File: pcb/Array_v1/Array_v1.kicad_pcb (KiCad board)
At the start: 4 copper layers, 430 parts, among them J1 D_ADC1, J11 D_VGA31, J12 D_VGA32, J13 D_ADC4, J14 GND, J16 D_VGA41, J17 D_VGA42, J18 VPOWER, J19 SPI_ADC, J2 MATCH1, J20 SPI_AGC_RX1, J21 SPI_AGC_RX2, J22 SPI_AGC_RX3, J23 SPI_AGC_RX4, J24 3.3VADC, J3 D_VGA11, J4 D_VGA11, J5 D_ADC2, J7 D_VGA21, J8 D_VGA22, J9 D_ADC3, U10 MEM, U11 DAC081S101, U12 AD8337, U13 ADS7040xDCU, U14 LMH6639, U15 CCSO-914X3-1000, U16 MAPD-009278, U17 MAPD-009278, U18 MAPD-009278, U19 CVSS-945-80.000, U2 TPS795, U20 MAPD-009278, U21 MAPD-009278, U22 MAPD-009278, U23 DAC081S101, U24 AD8337, U3 B39921, U4 SKY67159, U5 PAT0816, U6 PAT0816, U67 ADR391, U68 AD8541, U7 LT5526, U8 LT5526, U9 NFL

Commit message: can't run LVS meaningfully
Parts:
- removed the AE1 at (-81.4, 13.4)
- removed the AE1 at (-81.5, 166.5)
- removed the AE1 at (-234.6, 166.4)
- removed the AE1 at (-235.0, 12.8)
- removed the C10 at (-142.7, 66.7)
- removed the C10 at (-134.8, 105.2)
- removed the C10 at (-173.3, 113.1)
- removed the C10 at (-181.7, 74.1)
- removed the C11 at (-127.3, 50.7)
- removed the C11 at (-118.7, 120.6)
- removed the C11 at (-188.6, 129.2)
- removed the C11 at (-197.8, 58.8)
- removed the C12 at (-124.2, 48.2)
- removed the C12 at (-116.3, 123.7)
- removed the C12 at (-191.8, 131.6)
- removed the C12 at (-200.2, 55.6)
- removed the C13 at (-141.2, 78.5)
- removed the C13 at (-146.6, 106.7)
- removed the C13 at (-174.8, 101.4)
- removed the C13 at (-169.9, 72.6)
- removed the C14 at (-122.7, 60.0)
- removed the C14 at (-128.0, 125.2)
- removed the C14 at (-193.3, 119.9)
- removed the C14 at (-188.4, 54.1)
- removed the C15 at (-135.8, 69.1)
- removed the C15 at (-137.2, 112.1)
- removed the C15 at (-180.2, 110.7)
- removed the C15 at (-179.3, 67.2)
- removed the C16 at (-117.3, 50.6)
- removed the C16 at (-118.7, 130.6)
- removed the C16 at (-198.7, 129.2)
- removed the C16 at (-197.8, 48.7)
- removed the C17 at (-146.4, 78.3)
- removed the C17 at (-146.4, 101.5)
- removed the C17 at (-169.6, 101.5)
- removed the C17 at (-170.1, 77.8)
- removed the C18 at (-127.9, 59.8)
- removed the C18 at (-127.9, 120.0)
- removed the C18 at (-188.1, 120.0)
- removed the C18 at (-188.6, 59.3)
- removed the C19 at (-144.6, 75.1)
- removed the C19 at (-143.1, 103.3)
- removed the C19 at (-171.4, 104.8)
- removed the C19 at (-173.4, 76.0)
- removed the C20 at (-126.1, 56.6)
- removed the C20 at (-124.6, 121.8)
- removed the C20 at (-189.9, 123.3)
- removed the C20 at (-191.9, 57.5)
- removed the C21 at (-139.4, 65.5)
- removed the C21 at (-133.6, 108.5)
- removed the C21 at (-176.6, 114.3)
- removed the C21 at (-182.9, 70.8)
- removed the C22 at (-120.9, 47.0)
- removed the C22 at (-115.1, 127.0)
- removed the C22 at (-195.1, 132.8)
- removed the C22 at (-201.4, 52.3)
- removed the C23 at (-137.0, 76.5)
- removed the C23 at (-144.6, 110.9)
- removed the C23 at (-178.9, 103.3)
- removed the C23 at (-171.9, 68.5)
- removed the C24 at (-135.6, 75.1)
- removed the C24 at (-143.2, 112.3)
- removed the C24 at (-180.4, 104.7)
- removed the C24 at (-173.3, 67.0)
- removed the C25 at (-118.5, 58.0)
- removed the C25 at (-126.1, 129.4)
- removed the C25 at (-197.4, 121.8)
- removed the C25 at (-190.4, 50.0)
- removed the C26 at (-116.9, 56.4)
- removed the C26 at (-124.5, 131.0)
- removed the C26 at (-199.1, 123.4)
- removed the C26 at (-192.0, 48.3)
- removed the C27 at (-150.3, 74.7)
- removed the C27 at (-142.8, 97.6)
- removed the C27 at (-165.6, 105.1)
- removed the C27 at (-173.7, 81.8)
- removed the C28 at (-132.0, 56.0)
- removed the C28 at (-124.0, 115.9)
- removed the C28 at (-184.0, 123.9)
- removed the C28 at (-192.4, 63.4)
- removed the C29 at (-155.0, 47.0)
- removed the C29 at (-115.1, 92.9)
- removed the C29 at (-160.9, 132.8)
- removed the C29 at (-201.4, 86.5)
- removed the C30 at (-149.7, 49.8)
- removed the C30 at (-117.9, 98.2)
- removed the C30 at (-166.3, 130.0)
- removed the C30 at (-198.6, 81.1)
- removed the C31 at (-159.0, 55.3)
- removed the C31 at (-123.3, 88.9)
- removed the C31 at (-157.0, 124.6)
- removed the C31 at (-193.1, 90.4)
- removed the C32 at (-155.9, 59.7)
- removed the C32 at (-127.8, 92.0)
- removed the C32 at (-160.1, 120.1)
- removed the C32 at (-188.7, 87.3)
- removed the C33 at (-150.6, 58.8)
- removed the C33 at (-126.9, 97.3)
- removed the C33 at (-165.4, 121.0)
- removed the C33 at (-189.6, 82.0)
- removed the C34 at (-157.9, 26.4)
- removed the C34 at (-94.4, 90.1)
- removed the C34 at (-158.1, 153.5)
- removed the C34 at (-222.0, 89.3)
- removed the C47 at (-154.4, 30.1)
- removed the C47 at (-98.2, 93.5)
- removed the C47 at (-161.6, 149.7)
- removed the C47 at (-218.3, 85.8)
- removed the C48 at (-149.0, 32.8)
- removed the C48 at (-100.9, 98.9)
- removed the C48 at (-167.0, 147.0)
- removed the C48 at (-215.6, 80.4)
- removed the C49 at (-158.5, 38.9)
- removed the C49 at (-107.0, 89.4)
- removed the C49 at (-157.4, 140.9)
- removed the C49 at (-209.5, 90.0)
- removed the C5 at (-103.5, 29.2)
- removed the C5 at (-97.2, 144.4)
- removed the C5 at (-212.4, 150.7)
- removed the C5 at (-219.3, 35.0)
- removed the C50 at (-155.2, 42.7)
- removed the C50 at (-110.7, 92.7)
- removed the C50 at (-160.8, 137.2)
- removed the C50 at (-205.7, 86.6)
- removed the C51 at (-150.1, 41.8)
- removed the C51 at (-109.9, 97.8)
- removed the C51 at (-165.9, 138.0)
- removed the C51 at (-206.6, 81.5)
- removed the C6 at (-94.1, 26.0)
- removed the C6 at (-94.1, 153.8)
- removed the C6 at (-221.8, 153.8)
- removed the C6 at (-222.4, 25.5)
- removed the C7 at (-102.0, 33.9)
- removed the C7 at (-102.0, 145.9)
- removed the C7 at (-213.9, 145.9)
- removed the C7 at (-214.5, 33.5)
- removed the C8 at (-98.9, 23.8)
- removed the C8 at (-91.8, 149.0)
- removed the C8 at (-217.1, 156.1)
- removed the C8 at (-224.6, 30.3)
- removed the C9 at (-145.7, 68.9)
- removed the C9 at (-137.0, 102.2)
- removed the C9 at (-170.3, 110.9)
- removed the C9 at (-179.5, 77.1)
- removed the CG1 at (-148.2, 53.1)
- removed the CG1 at (-121.2, 99.7)
- removed the CG1 at (-167.8, 126.7)
- removed the CG1 at (-195.3, 79.6)
- removed the CG2 at (-147.6, 36.3)
- removed the CG2 at (-104.4, 100.3)
- removed the CG2 at (-168.4, 143.5)
- removed the CG2 at (-212.1, 79.0)
- removed the J1 at (-148.0, 9.27)
- removed the J1 at (-77.3, 99.9)
- removed the J1 at (-168.0, 170.6)
- removed the J1 at (-239.1, 79.4)
- removed J11: D_VGA31, Connector_Wire:SolderWirePad_1x01_Drill0.8mm
- removed J12: D_VGA32, Connector_Wire:SolderWirePad_1x01_Drill0.8mm
- removed J13: D_ADC4, Connector_Wire:SolderWirePad_1x01_Drill0.8mm
- removed J16: D_VGA41, Connector_Wire:SolderWirePad_1x01_Drill0.8mm
- removed J17: D_VGA42, Connector_Wire:SolderWirePad_1x01_Drill0.8mm
- removed the J19 at (-140.7, 9.27)
- removed the J19 at (-77.3, 107.2)
- removed the J19 at (-175.3, 170.6)
- removed the J19 at (-239.1, 72.1)
- removed the J2 at (-91.0, 23.0)
- removed the J2 at (-91.1, 156.9)
- removed the J2 at (-225.0, 156.8)
- removed the J2 at (-225.4, 22.4)
- removed the J20 at (-121.4, 9.14)
- removed the J20 at (-77.2, 126.5)
- removed the J20 at (-194.6, 170.7)
- removed the J20 at (-239.3, 52.8)
- removed J21: SPI_AGC_RX2, Connector_Wire:SolderWirePad_1x02_P3.81mm_Drill0.8mm
- removed J22: SPI_AGC_RX3, Connector_Wire:SolderWirePad_1x02_P3.81mm_Drill0.8mm
- removed J23: SPI_AGC_RX4, DFN8:SON50P200X200X80-9N
- removed the J3 at (-129.0, 9.14)
- removed the J3 at (-77.2, 118.9)
- removed the J3 at (-186.9, 170.7)
- removed the J3 at (-239.3, 60.5)
- removed the J4 at (-125.5, 9.14)
- removed the J4 at (-77.2, 122.4)
- removed the J4 at (-190.5, 170.7)
- removed the J4 at (-239.3, 56.9)
- removed J5: D_ADC2, Connector_Wire:SolderWirePad_1x01_Drill0.8mm
- removed J7: D_VGA21, Connector_Wire:SolderWirePad_1x01_Drill0.8mm
- removed J8: D_VGA22, Connector_Wire:SolderWirePad_1x01_Drill0.8mm
- removed J9: D_ADC3, Connector_Wire:SolderWirePad_1x01_Drill0.8mm
- removed the L1 at (-103.3, 31.5)
- removed the L1 at (-99.6, 144.6)
- removed the L1 at (-212.6, 148.3)
- removed the L1 at (-216.9, 34.8)
- removed the L10 at (-146.6, 72.0)
- removed the L10 at (-140.1, 101.3)
- removed the L10 at (-169.4, 107.8)
- removed the L10 at (-176.4, 78.0)
- removed the L11 at (-147.8, 75.8)
- removed the L11 at (-143.9, 100.1)
- removed the L11 at (-168.1, 104.0)
- removed the L11 at (-172.6, 79.3)
- removed the L12 at (-127.9, 53.7)
- removed the L12 at (-121.7, 120.0)
- removed the L12 at (-188.1, 126.2)
- removed the L12 at (-194.7, 59.3)
- removed the L13 at (-129.3, 57.3)
- removed the L13 at (-125.4, 118.6)
- removed the L13 at (-186.7, 122.5)
- removed the L13 at (-191.1, 60.7)
- removed the L14 at (-134.9, 65.7)
- removed the L14 at (-133.8, 113.0)
- removed the L14 at (-181.1, 114.1)
- removed the L14 at (-182.7, 66.3)
- removed the L15 at (-116.4, 47.2)
- removed the L15 at (-115.3, 131.5)
- removed the L15 at (-199.6, 132.6)
- removed the L15 at (-201.2, 47.8)
- removed the L16 at (-151.3, 47.0)
- removed the L16 at (-115.1, 96.6)
- removed the L16 at (-164.7, 132.8)
- removed the L16 at (-201.4, 82.7)
- removed the L17 at (-150.5, 30.1)
- removed the L17 at (-98.2, 97.4)
- removed the L17 at (-165.5, 149.7)
- removed the L17 at (-218.3, 81.9)
- removed the L2 at (-96.6, 28.5)
- removed the L2 at (-96.6, 151.3)
- removed the L2 at (-219.4, 151.3)
- removed the L2 at (-219.9, 28.0)
- removed the L3 at (-98.9, 27.4)
- removed the L3 at (-95.4, 149.0)
- removed the L3 at (-217.1, 152.5)
- removed the L3 at (-221.1, 30.3)
- removed the L4 at (-133.7, 72.4)
- removed the L4 at (-140.4, 114.2)
- removed the L4 at (-182.3, 107.5)
- removed the L4 at (-176.1, 65.1)
- removed the L5 at (-115.1, 53.9)
- removed the L5 at (-122.0, 132.8)
- removed the L5 at (-200.9, 125.9)
- removed the L5 at (-194.5, 46.5)
- removed the L6 at (-143.2, 76.5)
- removed the L6 at (-144.6, 104.7)
- removed the L6 at (-172.8, 103.3)
- removed the L6 at (-171.9, 74.6)
- removed the L7 at (-124.6, 58.0)
- removed the L7 at (-126.1, 123.3)
- removed the L7 at (-191.3, 121.8)
- removed the L7 at (-190.4, 56.1)
- removed the L8 at (-137.2, 67.7)
- removed the L8 at (-135.8, 110.7)
- removed the L8 at (-178.7, 112.1)
- removed the L8 at (-180.7, 68.7)
- removed the L9 at (-118.7, 49.2)
- removed the L9 at (-117.3, 129.2)
- removed the L9 at (-197.3, 130.6)
- removed the L9 at (-199.2, 50.1)
- removed the R1 at (-101.2, 26.1)
- removed the R1 at (-94.2, 146.7)
- removed the R1 at (-214.7, 153.7)
- removed the R1 at (-222.3, 32.6)
- removed the R13 at (-156.0, 38.9)
- removed the R13 at (-107.0, 91.9)
- removed the R13 at (-160.0, 140.9)
- removed the R13 at (-209.5, 87.4)
- removed the R14 at (-84.5, 16.5)
- removed the R14 at (-84.6, 163.4)
- removed the R14 at (-231.5, 163.3)
- removed the R14 at (-231.9, 15.9)
- removed the R15 at (-86.0, 18.0)
- removed the R15 at (-86.1, 161.9)
- removed the R15 at (-230.0, 161.8)
- removed the R15 at (-230.4, 17.4)
- removed the R16 at (-83.9, 14.7)
- removed the R16 at (-82.8, 164.0)
- removed the R16 at (-232.1, 165.1)
- removed the R16 at (-233.7, 15.3)
- removed the R17 at (-83.5, 14.3)
- removed the R17 at (-82.4, 164.5)
- removed the R17 at (-232.5, 165.6)
- removed the R17 at (-234.1, 14.9)
- removed the R18 at (-86.7, 19.8)
- removed the R18 at (-87.9, 161.2)
- removed the R18 at (-229.3, 160.0)
- removed the R18 at (-228.6, 18.1)
- removed the R19 at (-87.1, 20.2)
- removed the R19 at (-88.3, 160.8)
- removed the R19 at (-228.9, 159.6)
- removed the R19 at (-228.2, 18.5)
- removed the R2 at (-156.3, 55.4)
- removed the R2 at (-123.5, 91.6)
- removed the R2 at (-159.6, 124.4)
- removed the R2 at (-193.0, 87.8)
- removed the R3 at (-160.9, 26.3)
- removed the R3 at (-94.4, 87.0)
- removed the R3 at (-155.1, 153.5)
- removed the R3 at (-222.1, 92.3)
- removed the R4 at (-156.5, 18.7)
- removed the R4 at (-86.8, 91.4)
- removed the R4 at (-159.5, 161.1)
- removed the R4 at (-229.7, 87.9)
- removed the R5 at (-153.8, 18.0)
- removed the R5 at (-86.1, 94.1)
- removed the R5 at (-162.2, 161.8)
- removed the R5 at (-230.4, 85.2)
- removed the R6 at (-154.8, 26.4)
- removed the R6 at (-94.4, 93.1)
- removed the R6 at (-161.2, 153.5)
- removed the R6 at (-222.0, 86.2)
- removed the RFB1 at (-151.1, 55.0)
- removed the RFB1 at (-123.1, 96.8)
- removed the RFB1 at (-164.9, 124.8)
- removed the RFB1 at (-193.4, 82.5)
- removed the RFB2 at (-153.4, 57.0)
- removed the RFB2 at (-125.1, 94.5)
- removed the RFB2 at (-162.6, 122.8)
- removed the RFB2 at (-191.4, 84.8)
- removed the RFB3 at (-150.2, 38.4)
- removed the RFB3 at (-106.5, 97.7)
- removed the RFB3 at (-165.7, 141.5)
- removed the RFB3 at (-210.0, 81.7)
- removed the RFB4 at (-152.8, 40.0)
- removed the RFB4 at (-108.1, 95.1)
- removed the RFB4 at (-163.2, 139.8)
- removed the RFB4 at (-208.4, 84.2)
- removed the RV1 at (-158.6, 49.1)
- removed the RV1 at (-117.1, 89.3)
- removed the RV1 at (-157.4, 130.8)
- removed the RV1 at (-199.4, 90.0)
- removed the RV2 at (-157.9, 32.3)
- removed the RV2 at (-100.4, 90.1)
- removed the RV2 at (-158.1, 147.5)
- removed the RV2 at (-216.1, 89.3)
- removed the U10 at (-131.3, 63.2)
- removed the U10 at (-131.3, 116.6)
- removed the U10 at (-184.7, 116.6)
- removed the U10 at (-185.2, 62.7)
- removed the U11 at (-142.7, 50.9)
- removed the U11 at (-119.0, 105.2)
- removed the U11 at (-173.2, 128.9)
- removed the U11 at (-197.5, 74.2)
- removed the U12 at (-154.5, 52.1)
- removed the U12 at (-120.2, 93.4)
- removed the U12 at (-161.4, 127.7)
- removed the U12 at (-196.3, 86.0)
- removed the U13 at (-157.4, 14.5)
- removed the U13 at (-82.5, 90.6)
- removed the U13 at (-158.6, 165.4)
- removed the U13 at (-233.9, 88.8)
- removed the U14 at (-156.4, 22.1)
- removed the U14 at (-90.2, 91.5)
- removed the U14 at (-159.6, 157.7)
- removed the U14 at (-226.3, 87.8)
- removed the U23 at (-142.5, 34.2)
- removed the U23 at (-102.2, 105.4)
- removed the U23 at (-173.5, 145.7)
- removed the U23 at (-214.2, 73.9)
- removed the U24 at (-153.5, 35.4)
- removed the U24 at (-103.4, 94.4)
- removed the U24 at (-162.4, 144.5)
- removed the U24 at (-213.0, 85.0)
- removed the U3 at (-108.8, 40.7)
- removed the U3 at (-108.8, 139.1)
- removed the U3 at (-207.1, 139.1)
- removed the U3 at (-207.7, 40.3)
- removed the U4 at (-99.5, 31.1)
- removed the U4 at (-99.1, 148.4)
- removed the U4 at (-216.5, 148.8)
- removed the U4 at (-217.3, 30.9)
- removed the U5 at (-105.5, 36.5)
- removed the U5 at (-104.6, 142.4)
- removed the U5 at (-210.5, 143.3)
- removed the U5 at (-211.9, 36.9)
- removed the U6 at (-113.0, 44.1)
- removed the U6 at (-112.2, 134.9)
- removed the U6 at (-202.9, 135.8)
- removed the U6 at (-204.3, 44.5)
- removed the U7 at (-140.1, 72.0)
- removed the U7 at (-140.1, 107.8)
- removed the U7 at (-175.9, 107.8)
- removed the U7 at (-176.4, 71.5)
- removed the U8 at (-121.6, 53.5)
- removed the U8 at (-121.6, 126.3)
- removed the U8 at (-194.4, 126.3)
- removed the U8 at (-194.9, 53.0)
- removed the U9 at (-155.4, 75.9)
- removed the U9 at (-144.0, 92.5)
- removed the U9 at (-160.5, 103.9)
- removed the U9 at (-172.5, 86.9)
- added AE1: Antenna, footprints:0915AT43A0026, F.Cu at (-81.0, 13.1)
- added AE1: Antenna, footprints:0915AT43A0026, F.Cu at (-81.1, 167.0)
- added AE1: Antenna, footprints:0915AT43A0026, F.Cu at (-235.0, 166.9)
- added AE1: Antenna, footprints:0915AT43A0026, F.Cu at (-234.9, 13.1)
- added C10: 2.2u, Capacitor_SMD:C_0805_2012Metric, F.Cu at (-142.3, 66.4)
- added C10: 2.2u, Capacitor_SMD:C_0805_2012Metric, F.Cu at (-134.4, 105.7)
- added C10: 2.2u, Capacitor_SMD:C_0805_2012Metric, F.Cu at (-173.7, 113.7)
- added C10: 2.2u, Capacitor_SMD:C_0805_2012Metric, F.Cu at (-181.6, 74.4)
- added C11: 0.01p, Capacitor_SMD:C_0603_1608Metric, F.Cu at (-127.0, 50.4)
- added C11: 0.01p, Capacitor_SMD:C_0603_1608Metric, F.Cu at (-118.4, 121.1)
- added C11: 0.01p, Capacitor_SMD:C_0603_1608Metric, F.Cu at (-189.0, 129.7)
- added C11: 0.01p, Capacitor_SMD:C_0603_1608Metric, F.Cu at (-197.6, 59.0)
- added C12: 2.2u, Capacitor_SMD:C_0805_2012Metric, F.Cu at (-123.8, 47.9)
- added C12: 2.2u, Capacitor_SMD:C_0805_2012Metric, F.Cu at (-115.9, 124.2)
- added C12: 2.2u, Capacitor_SMD:C_0805_2012Metric, F.Cu at (-192.2, 132.2)
- added C12: 2.2u, Capacitor_SMD:C_0805_2012Metric, F.Cu at (-200.1, 55.9)
- added C13: 180p, Capacitor_SMD:C_0603_1608Metric, F.Cu at (-140.8, 78.2)
- added C13: 180p, Capacitor_SMD:C_0603_1608Metric, F.Cu at (-146.2, 107.2)
- added C13: 180p, Capacitor_SMD:C_0603_1608Metric, F.Cu at (-175.2, 101.9)
- added C13: 180p, Capacitor_SMD:C_0603_1608Metric, F.Cu at (-169.8, 72.9)
- added C14: 11p, Capacitor_SMD:C_0603_1608Metric, F.Cu at (-122.3, 59.7)
- added C14: 11p, Capacitor_SMD:C_0603_1608Metric, F.Cu at (-127.7, 125.7)
- added C14: 11p, Capacitor_SMD:C_0603_1608Metric, F.Cu at (-193.7, 120.4)
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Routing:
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- added copper zone on B.Cu, net GND
- added copper zone on F.Cu, net GND
- added copper zone on In1.Cu, net GND
- added copper zone on In2.Cu, net GND
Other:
- board outline added: 173.9 x 173.9 mm

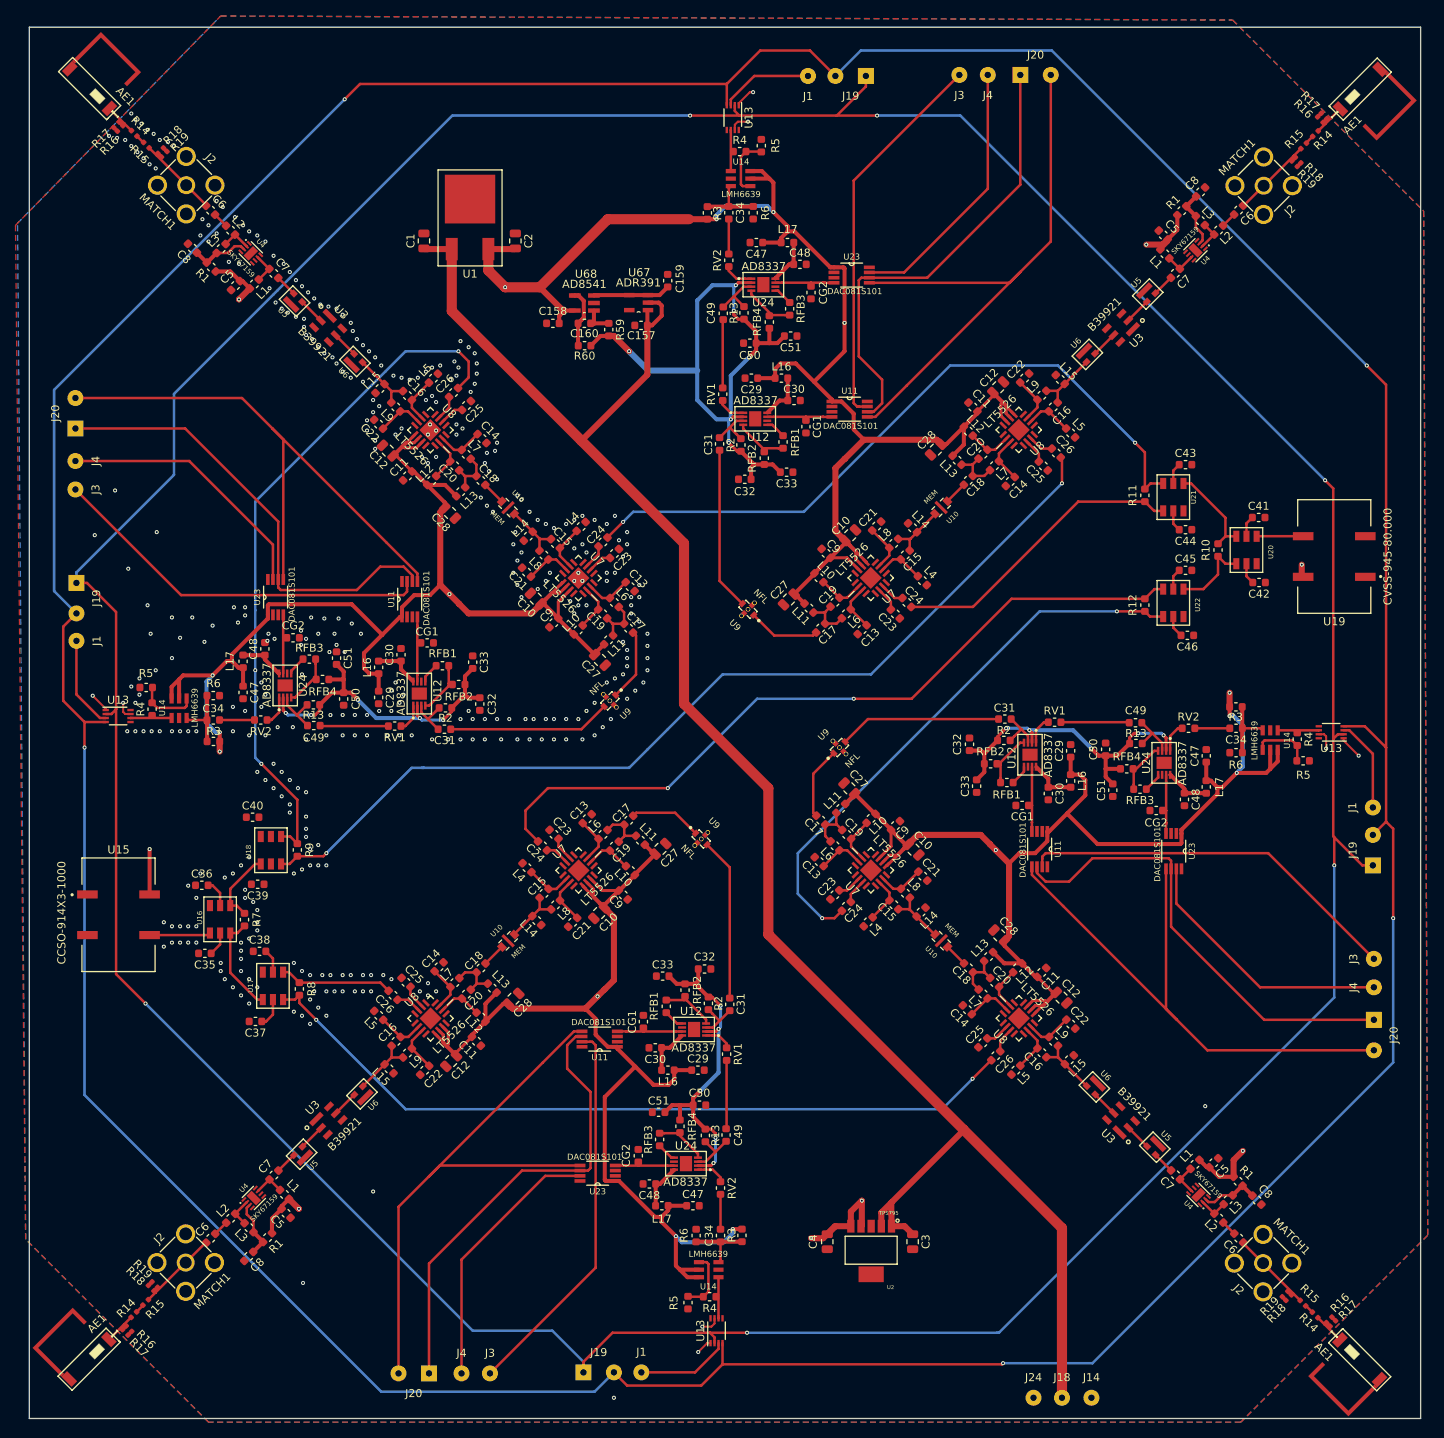
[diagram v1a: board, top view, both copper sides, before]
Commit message: added all gnd vias
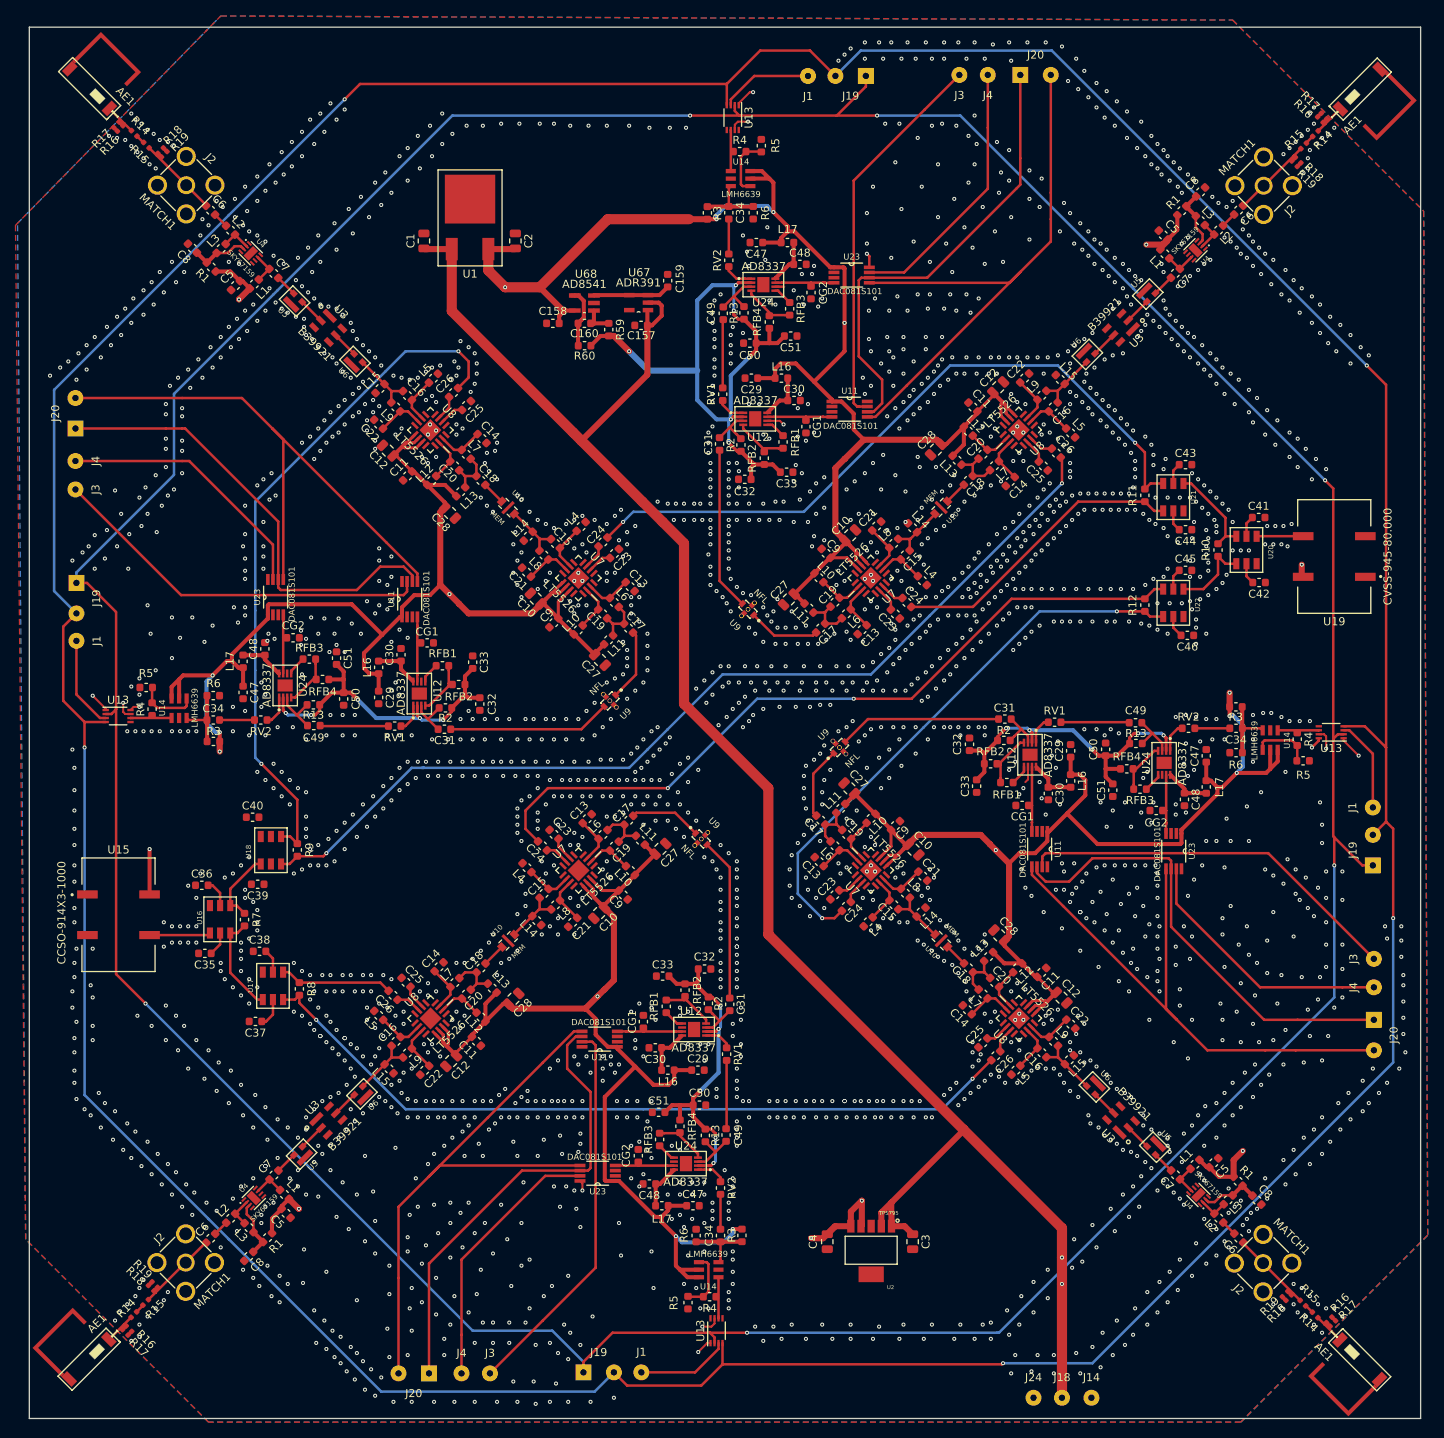
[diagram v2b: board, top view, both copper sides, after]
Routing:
- net +5V: track 900.2 -> 884.3 mm
- net GND: track 4.96 -> 16.3 mm, vias 354 -> 2573
- net +3V3: vias 16 -> 17
- net VAA: vias 0 -> 2
- net LO14: vias 3 -> 2

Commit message: passed DRC
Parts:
- removed the AE1 at (-81.0, 13.1)
- removed the AE1 at (-81.1, 167.0)
- removed the AE1 at (-235.0, 166.9)
- removed the C10 at (-142.3, 66.4)
- removed the C10 at (-134.4, 105.7)
- removed the C10 at (-173.7, 113.7)
- removed the C11 at (-127.0, 50.4)
- removed the C11 at (-118.4, 121.1)
- removed the C11 at (-189.0, 129.7)
- removed the C12 at (-123.8, 47.9)
- removed the C12 at (-115.9, 124.2)
- removed the C12 at (-192.2, 132.2)
- removed the C13 at (-140.8, 78.2)
- removed the C13 at (-146.2, 107.2)
- removed the C13 at (-175.2, 101.9)
- removed the C14 at (-122.3, 59.7)
- removed the C14 at (-127.7, 125.7)
- removed the C14 at (-193.7, 120.4)
- removed the C15 at (-135.4, 68.9)
- removed the C15 at (-136.8, 112.6)
- removed the C15 at (-180.6, 111.2)
- removed the C16 at (-116.9, 50.4)
- removed the C16 at (-118.3, 131.1)
- removed the C16 at (-199.1, 129.7)
- removed the C17 at (-146.0, 78.0)
- removed the C17 at (-146.0, 102.0)
- removed the C17 at (-170.0, 102.1)
- removed the C18 at (-127.5, 59.6)
- removed the C18 at (-127.5, 120.5)
- removed the C18 at (-188.4, 120.5)
- removed the C19 at (-144.2, 74.8)
- removed the C19 at (-142.7, 103.8)
- removed the C19 at (-171.8, 105.3)
- removed the C20 at (-125.7, 56.3)
- removed the C20 at (-124.2, 122.3)
- removed the C20 at (-190.3, 123.8)
- removed the C21 at (-139.0, 65.3)
- removed the C21 at (-133.2, 109.0)
- removed the C21 at (-177.0, 114.8)
- removed the C22 at (-120.5, 46.8)
- removed the C22 at (-114.7, 127.5)
- removed the C22 at (-195.5, 133.3)
- removed the C23 at (-136.7, 76.3)
- removed the C23 at (-144.2, 111.4)
- removed the C23 at (-179.3, 103.8)
- removed the C24 at (-135.2, 74.8)
- removed the C24 at (-142.8, 112.8)
- removed the C24 at (-180.8, 105.3)
- removed the C25 at (-118.2, 57.8)
- removed the C25 at (-125.7, 129.9)
- removed the C25 at (-197.8, 122.3)
- removed the C26 at (-116.5, 56.2)
- removed the C26 at (-124.1, 131.5)
- removed the C26 at (-199.4, 123.9)
- removed the C27 at (-150.0, 74.5)
- removed the C27 at (-142.4, 98.1)
- removed the C27 at (-166.0, 105.6)
- removed the C28 at (-131.6, 55.7)
- removed the C28 at (-123.7, 116.4)
- removed the C28 at (-184.4, 124.4)
- removed the C29 at (-154.6, 46.8)
- removed the C29 at (-114.7, 93.4)
- removed the C30 at (-149.3, 49.6)
- removed the C30 at (-117.5, 98.7)
- removed the C30 at (-166.7, 130.5)
- removed the C31 at (-158.6, 55.0)
- removed the C31 at (-123.0, 89.4)
- removed the C31 at (-157.4, 125.1)
- removed the C32 at (-155.5, 59.4)
- removed the C32 at (-127.4, 92.6)
- removed the C32 at (-160.5, 120.7)
- removed the C33 at (-150.2, 58.5)
- removed the C33 at (-126.5, 97.8)
- removed the C33 at (-165.7, 121.5)
- removed the C34 at (-157.5, 26.1)
- removed the C34 at (-94.1, 90.6)
- removed the C34 at (-158.5, 154.0)
- removed the C47 at (-154.0, 29.8)
- removed the C47 at (-97.8, 94.0)
- removed the C47 at (-162.0, 150.2)
- removed the C48 at (-148.6, 32.6)
- removed the C48 at (-100.5, 99.5)
- removed the C48 at (-167.4, 147.5)
- removed the C49 at (-158.2, 38.7)
- removed the C49 at (-106.6, 89.9)
- removed the C49 at (-157.8, 141.4)
- removed the C5 at (-103.2, 28.9)
- removed the C5 at (-96.8, 144.9)
- removed the C5 at (-212.8, 151.2)
- removed the C50 at (-154.8, 42.4)
- removed the C50 at (-110.4, 93.2)
- removed the C50 at (-161.1, 137.7)
- removed the C51 at (-149.7, 41.5)
- removed the C51 at (-109.5, 98.3)
- removed the C51 at (-166.2, 138.6)
- removed the C6 at (-93.7, 25.8)
- removed the C6 at (-93.7, 154.3)
- removed the C6 at (-222.2, 154.3)
- removed the C7 at (-101.6, 33.7)
- removed the C7 at (-101.6, 146.4)
- removed the C7 at (-214.3, 146.4)
- removed the C8 at (-98.5, 23.5)
- removed the C8 at (-91.5, 149.5)
- removed the C8 at (-217.5, 156.6)
- removed the C9 at (-145.3, 68.7)
- removed the C9 at (-136.6, 102.7)
- removed the C9 at (-170.7, 111.4)
- removed the CG1 at (-147.8, 52.9)
- removed the CG1 at (-120.8, 100.2)
- removed the CG1 at (-168.1, 127.2)
- removed the CG2 at (-147.2, 36.1)
- removed the CG2 at (-104.0, 100.8)
- removed the CG2 at (-168.8, 144.0)
- removed the J1 at (-147.6, 9.02)
- removed the J1 at (-77.0, 100.5)
- removed the J1 at (-168.4, 171.1)
- removed the J2 at (-90.6, 22.7)
- removed the J2 at (-90.7, 157.4)
- removed the J2 at (-225.4, 157.3)
- removed the J20 at (-121.0, 8.89)
- removed the J20 at (-76.8, 127.0)
- removed the J20 at (-194.9, 171.2)
- removed the J3 at (-128.7, 8.89)
- removed the J3 at (-76.8, 119.4)
- removed the J3 at (-187.3, 171.2)
- removed the J4 at (-125.1, 8.89)
- removed the J4 at (-76.8, 122.9)
- removed the J4 at (-190.9, 171.2)
- removed the L1 at (-103.0, 31.3)
- removed the L1 at (-99.2, 145.1)
- removed the L1 at (-213.0, 148.8)
- removed the L10 at (-146.2, 71.7)
- removed the L10 at (-139.7, 101.8)
- removed the L10 at (-169.8, 108.3)
- removed the L11 at (-147.4, 75.5)
- removed the L11 at (-143.5, 100.6)
- removed the L11 at (-168.5, 104.6)
- removed the L12 at (-127.5, 53.4)
- removed the L12 at (-121.4, 120.5)
- removed the L12 at (-188.4, 126.7)
- removed the L13 at (-128.9, 57.1)
- removed the L13 at (-125.0, 119.1)
- removed the L13 at (-187.0, 123.0)
- removed the L14 at (-134.5, 65.5)
- removed the L14 at (-133.4, 113.5)
- removed the L14 at (-181.5, 114.6)
- removed the L15 at (-116.0, 47.0)
- removed the L15 at (-114.9, 132.0)
- removed the L15 at (-199.9, 133.1)
- removed the L16 at (-150.9, 46.8)
- removed the L16 at (-114.7, 97.1)
- removed the L16 at (-165.1, 133.3)
- removed the L17 at (-150.1, 29.8)
- removed the L17 at (-97.8, 97.9)
- removed the L17 at (-165.8, 150.2)
- removed the L2 at (-96.2, 28.3)
- removed the L2 at (-96.2, 151.8)
- removed the L2 at (-219.7, 151.8)
- removed the L3 at (-98.5, 27.1)
- removed the L3 at (-95.1, 149.5)
- removed the L3 at (-217.4, 153.0)
- removed the L4 at (-133.3, 72.1)
- removed the L4 at (-140.0, 114.8)
- removed the L4 at (-182.7, 108.0)
- removed the L5 at (-114.7, 53.6)
- removed the L5 at (-121.6, 133.3)
- removed the L5 at (-201.2, 126.4)
- removed the L6 at (-142.8, 76.3)
- removed the L6 at (-144.2, 105.3)
- removed the L6 at (-173.2, 103.8)
- removed the L7 at (-124.3, 57.7)
- removed the L7 at (-125.7, 123.8)
- removed the L7 at (-191.7, 122.4)
- removed the L8 at (-136.9, 67.5)
- removed the L8 at (-135.4, 111.2)
- removed the L8 at (-179.1, 112.6)
- removed the L9 at (-118.3, 48.9)
- removed the L9 at (-116.9, 129.7)
- removed the L9 at (-197.6, 131.2)
- removed the R1 at (-100.8, 25.9)
- removed the R1 at (-93.8, 147.2)
- removed the R1 at (-215.1, 154.2)
- removed the R13 at (-155.6, 38.6)
- removed the R13 at (-106.6, 92.5)
- removed the R13 at (-160.4, 141.5)
- removed the R14 at (-84.1, 16.2)
- removed the R14 at (-84.2, 163.9)
- removed the R14 at (-231.8, 163.8)
- removed the R15 at (-85.6, 17.8)
- removed the R15 at (-85.7, 162.4)
- removed the R15 at (-230.4, 162.3)
- removed the R16 at (-83.5, 14.5)
- removed the R16 at (-82.4, 164.5)
- removed the R16 at (-232.5, 165.6)
- removed the R17 at (-83.1, 14.0)
- removed the R17 at (-82.0, 165.0)
- removed the R17 at (-232.9, 166.1)
- removed the R18 at (-86.3, 19.6)
- removed the R18 at (-87.5, 161.7)
- removed the R18 at (-229.7, 160.5)
- removed the R19 at (-86.7, 20.0)
- removed the R19 at (-87.9, 161.3)
- removed the R19 at (-229.2, 160.1)
- removed the R2 at (-156.0, 55.1)
- removed the R2 at (-123.1, 92.1)
- removed the R2 at (-160.0, 124.9)
- removed the R3 at (-160.1, 26.1)
- removed the R3 at (-94.1, 87.9)
- removed the R3 at (-155.8, 153.9)
- removed the R4 at (-156.1, 18.5)
- removed the R4 at (-86.4, 91.9)
- removed the R4 at (-159.9, 161.6)
- removed the R5 at (-153.4, 17.7)
- removed the R5 at (-85.7, 94.6)
- removed the R5 at (-162.6, 162.4)
- removed the R6 at (-154.4, 26.1)
- removed the R6 at (-94.1, 93.6)
- removed the R6 at (-161.6, 154.0)
- removed the RFB1 at (-150.7, 54.8)
- removed the RFB1 at (-122.7, 97.3)
- removed the RFB1 at (-165.3, 125.3)
- removed the RFB2 at (-153.0, 56.8)
- removed the RFB2 at (-124.7, 95.0)
- removed the RFB2 at (-162.9, 123.3)
- removed the RFB3 at (-149.9, 38.1)
- removed the RFB3 at (-106.1, 98.2)
- removed the RFB3 at (-166.1, 142.0)
- removed the RFB4 at (-152.4, 39.8)
- removed the RFB4 at (-107.7, 95.6)
- removed the RFB4 at (-163.6, 140.3)
- removed the RV1 at (-158.2, 48.8)
- removed the RV1 at (-116.7, 89.8)
- removed the RV1 at (-157.7, 131.3)
- removed the RV2 at (-157.5, 32.1)
- removed the RV2 at (-100.0, 90.6)
- removed the RV2 at (-158.5, 148.0)
- removed the U10 at (-130.9, 63.0)
- removed the U10 at (-130.9, 117.1)
- removed the U10 at (-185.1, 117.1)
- removed the U11 at (-142.4, 50.7)
- removed the U11 at (-118.6, 105.7)
- removed the U11 at (-173.6, 129.4)
- removed the U12 at (-154.2, 51.9)
- removed the U12 at (-119.8, 93.9)
- removed the U12 at (-161.8, 128.2)
- removed the U13 at (-157.0, 14.2)
- removed the U13 at (-82.2, 91.1)
- removed the U13 at (-159.0, 165.9)
- removed the U14 at (-156.0, 21.8)
- removed the U14 at (-89.8, 92.0)
- removed the U14 at (-160.0, 158.2)
- removed the U23 at (-142.1, 33.9)
- removed the U23 at (-101.9, 105.9)
- removed the U23 at (-173.9, 146.2)
- removed the U24 at (-153.2, 35.1)
- removed the U24 at (-103.1, 94.9)
- removed the U24 at (-162.8, 145.0)
- removed the U3 at (-108.5, 40.5)
- removed the U3 at (-108.4, 139.6)
- removed the U3 at (-207.5, 139.6)
- removed the U4 at (-99.1, 30.8)
- removed the U4 at (-98.8, 148.9)
- removed the U4 at (-216.8, 149.3)
- removed the U5 at (-105.1, 36.3)
- removed the U5 at (-104.2, 142.9)
- removed the U5 at (-210.9, 143.8)
- removed the U6 at (-112.6, 43.8)
- removed the U6 at (-111.8, 135.4)
- removed the U6 at (-203.3, 136.3)
- removed the U7 at (-139.7, 71.8)
- removed the U7 at (-139.7, 108.3)
- removed the U7 at (-176.2, 108.3)
- removed the U8 at (-121.2, 53.3)
- removed the U8 at (-121.2, 126.8)
- removed the U8 at (-194.7, 126.8)
- removed the U9 at (-155.1, 75.7)
- removed the U9 at (-143.6, 93.0)
- removed the U9 at (-160.9, 104.4)
- added AE2: Antenna, footprints:0915AT43A0026, F.Cu at (40.9, 182.4)
- added AE3: Antenna, footprints:0915AT43A0026, F.Cu at (194.8, 182.5)
- added AE4: Antenna, footprints:0915AT43A0026, F.Cu at (194.9, 28.6)
- added C100: 0.1u, Capacitor_SMD:C_0603_1608Metric, F.Cu at (148.4, 136.0)
- added C101: 180p, Capacitor_SMD:C_0603_1608Metric, F.Cu at (133.1, 119.3)
- added C102: 11p, Capacitor_SMD:C_0603_1608Metric, F.Cu at (151.7, 137.8)
- added C103: 47p, Capacitor_SMD:C_0603_1608Metric, F.Cu at (142.7, 124.5)
- added C104: 4.4p, Capacitor_SMD:C_0603_1608Metric, F.Cu at (161.2, 143.0)
- added C105: 0.1u, Capacitor_SMD:C_0603_1608Metric, F.Cu at (131.7, 126.9)
- added C106: 0.1u, Capacitor_SMD:C_0603_1608Metric, F.Cu at (133.1, 128.3)
- added C107: 100p, Capacitor_SMD:C_0603_1608Metric, F.Cu at (150.2, 145.4)
- added C108: 100p, Capacitor_SMD:C_0603_1608Metric, F.Cu at (151.8, 147.0)
- added C109: 2.2u, Capacitor_SMD:C_0805_2012Metric, F.Cu at (133.5, 113.6)
- added C110: 2.2u, Capacitor_SMD:C_0805_2012Metric, F.Cu at (152.2, 131.9)
- added C111: 10u, Capacitor_SMD:C_0603_1608Metric, F.Cu at (161.2, 108.9)
- added C112: 0.1u, Capacitor_SMD:C_0603_1608Metric, F.Cu at (158.4, 114.2)
- added C113: 0.1u, Capacitor_SMD:C_0603_1608Metric, F.Cu at (152.9, 104.9)
- added C114: 1u, Capacitor_SMD:C_0603_1608Metric, F.Cu at (148.5, 108.1)
- added C115: 0.1u, Capacitor_SMD:C_0603_1608Metric, F.Cu at (149.4, 113.3)
- added C116: 1u, Capacitor_SMD:C_0603_1608Metric, F.Cu at (181.8, 106.0)
- added C117: 10u, Capacitor_SMD:C_0603_1608Metric, F.Cu at (178.1, 109.5)
- added C118: 0.1u, Capacitor_SMD:C_0603_1608Metric, F.Cu at (175.4, 114.9)
- added C119: 0.1u, Capacitor_SMD:C_0603_1608Metric, F.Cu at (169.3, 105.4)
- added C120: 1u, Capacitor_SMD:C_0603_1608Metric, F.Cu at (165.5, 108.7)
- added C121: 0.1u, Capacitor_SMD:C_0603_1608Metric, F.Cu at (166.4, 113.8)
- added C122: 100p, Capacitor_SMD:C_0603_1608Metric, F.Cu at (172.7, 44.4)
- added C123: 100p, Capacitor_SMD:C_0603_1608Metric, F.Cu at (182.1, 41.3)
- added C124: 100p, Capacitor_SMD:C_0603_1608Metric, F.Cu at (174.2, 49.2)
- added C125: 100p, Capacitor_SMD:C_0603_1608Metric, F.Cu at (177.4, 39.0)
- added C126: 0.01p, Capacitor_SMD:C_0603_1608Metric, F.Cu at (148.9, 65.9)
- added C127: 2.2u, Capacitor_SMD:C_0805_2012Metric, F.Cu at (133.6, 81.9)
- added C128: 0.01p, Capacitor_SMD:C_0603_1608Metric, F.Cu at (130.6, 84.2)
- added C129: 2.2u, Capacitor_SMD:C_0805_2012Metric, F.Cu at (152.1, 63.4)
- added C130: 180p, Capacitor_SMD:C_0603_1608Metric, F.Cu at (135.1, 93.7)
- added C131: 11p, Capacitor_SMD:C_0603_1608Metric, F.Cu at (153.6, 75.2)
- added C132: 47p, Capacitor_SMD:C_0603_1608Metric, F.Cu at (140.5, 84.4)
- added C133: 4.4p, Capacitor_SMD:C_0603_1608Metric, F.Cu at (159.0, 65.9)
- added C134: 1u, Capacitor_SMD:C_0603_1608Metric, F.Cu at (129.9, 93.5)
- added C135: 0.1u, Capacitor_SMD:C_0603_1608Metric, F.Cu at (148.4, 75.1)
- added C136: 180p, Capacitor_SMD:C_0603_1608Metric, F.Cu at (131.7, 90.3)
- added C137: 11p, Capacitor_SMD:C_0603_1608Metric, F.Cu at (150.2, 71.8)
- added C138: 47p, Capacitor_SMD:C_0603_1608Metric, F.Cu at (136.9, 80.8)
- added C139: 4.4p, Capacitor_SMD:C_0603_1608Metric, F.Cu at (155.4, 62.3)
- added C140: 0.1u, Capacitor_SMD:C_0603_1608Metric, F.Cu at (139.2, 91.8)
- added C141: 0.1u, Capacitor_SMD:C_0603_1608Metric, F.Cu at (140.7, 90.3)
- added C142: 100p, Capacitor_SMD:C_0603_1608Metric, F.Cu at (157.7, 73.3)
- added C143: 100p, Capacitor_SMD:C_0603_1608Metric, F.Cu at (159.4, 71.7)
- added C144: 2.2u, Capacitor_SMD:C_0805_2012Metric, F.Cu at (125.9, 89.9)
- added C145: 2.2u, Capacitor_SMD:C_0805_2012Metric, F.Cu at (144.3, 71.2)
- added C146: 10u, Capacitor_SMD:C_0603_1608Metric, F.Cu at (121.3, 62.3)
- added C147: 0.1u, Capacitor_SMD:C_0603_1608Metric, F.Cu at (126.6, 65.1)
- added C148: 0.1u, Capacitor_SMD:C_0603_1608Metric, F.Cu at (117.3, 70.5)
- added C149: 1u, Capacitor_SMD:C_0603_1608Metric, F.Cu at (120.4, 74.9)
- added C150: 0.1u, Capacitor_SMD:C_0603_1608Metric, F.Cu at (125.7, 74.0)
- added C151: 1u, Capacitor_SMD:C_0603_1608Metric, F.Cu at (118.4, 41.6)
- added C152: 10u, Capacitor_SMD:C_0603_1608Metric, F.Cu at (121.9, 45.3)
- added C153: 0.1u, Capacitor_SMD:C_0603_1608Metric, F.Cu at (127.3, 48.1)
- added C154: 0.1u, Capacitor_SMD:C_0603_1608Metric, F.Cu at (117.7, 54.2)
- added C155: 1u, Capacitor_SMD:C_0603_1608Metric, F.Cu at (121.1, 57.9)
- added C156: 0.1u, Capacitor_SMD:C_0603_1608Metric, F.Cu at (126.2, 57.0)
- added C52: 100p, Capacitor_SMD:C_0603_1608Metric, F.Cu at (63.1, 166.7)
- added C53: 100p, Capacitor_SMD:C_0603_1608Metric, F.Cu at (53.7, 169.8)
- added C54: 100p, Capacitor_SMD:C_0603_1608Metric, F.Cu at (61.6, 161.9)
- added C55: 100p, Capacitor_SMD:C_0603_1608Metric, F.Cu at (58.4, 172.1)
- added C56: 0.01p, Capacitor_SMD:C_0603_1608Metric, F.Cu at (105.2, 126.9)
- added C57: 2.2u, Capacitor_SMD:C_0805_2012Metric, F.Cu at (102.2, 129.2)
- added C58: 0.01p, Capacitor_SMD:C_0603_1608Metric, F.Cu at (86.9, 145.2)
- added C59: 2.2u, Capacitor_SMD:C_0805_2012Metric, F.Cu at (83.7, 147.7)
- added C60: 180p, Capacitor_SMD:C_0603_1608Metric, F.Cu at (100.7, 117.3)
- added C61: 11p, Capacitor_SMD:C_0603_1608Metric, F.Cu at (82.2, 135.8)
- added C62: 47p, Capacitor_SMD:C_0603_1608Metric, F.Cu at (95.3, 126.7)
- added C63: 4.4p, Capacitor_SMD:C_0603_1608Metric, F.Cu at (76.8, 145.2)
- added C64: 1u, Capacitor_SMD:C_0603_1608Metric, F.Cu at (105.9, 117.6)
- added C65: 0.1u, Capacitor_SMD:C_0603_1608Metric, F.Cu at (87.4, 136.0)
- added C66: 180p, Capacitor_SMD:C_0603_1608Metric, F.Cu at (104.1, 120.8)
- added C67: 11p, Capacitor_SMD:C_0603_1608Metric, F.Cu at (85.6, 139.3)
- added C68: 47p, Capacitor_SMD:C_0603_1608Metric, F.Cu at (98.9, 130.3)
- added C69: 4.4p, Capacitor_SMD:C_0603_1608Metric, F.Cu at (80.4, 148.8)
- added C70: 0.1u, Capacitor_SMD:C_0603_1608Metric, F.Cu at (96.6, 119.3)
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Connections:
- C26 pad 1: LO14 -> LO11
- R11 pad 2: LO22 -> LO24
- R12 pad 1: LO23 -> LO22
- R12 pad 2: LO24 -> LO23
- R8 pad 1: LO11 -> LO13
- R9 pad 1: LO13 -> LO14
- R9 pad 2: LO14 -> LO11
- U17 pad 3: LO11 -> LO13
- U18 pad 3: LO13 -> LO14
- U18 pad 4: LO14 -> LO11
- U21 pad 4: LO22 -> LO24
- U22 pad 3: LO23 -> LO22
- U22 pad 4: LO24 -> LO23
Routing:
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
